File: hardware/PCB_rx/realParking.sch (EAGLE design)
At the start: 14 parts, among them IC1 MEGA8-P, IC2 LD117AV

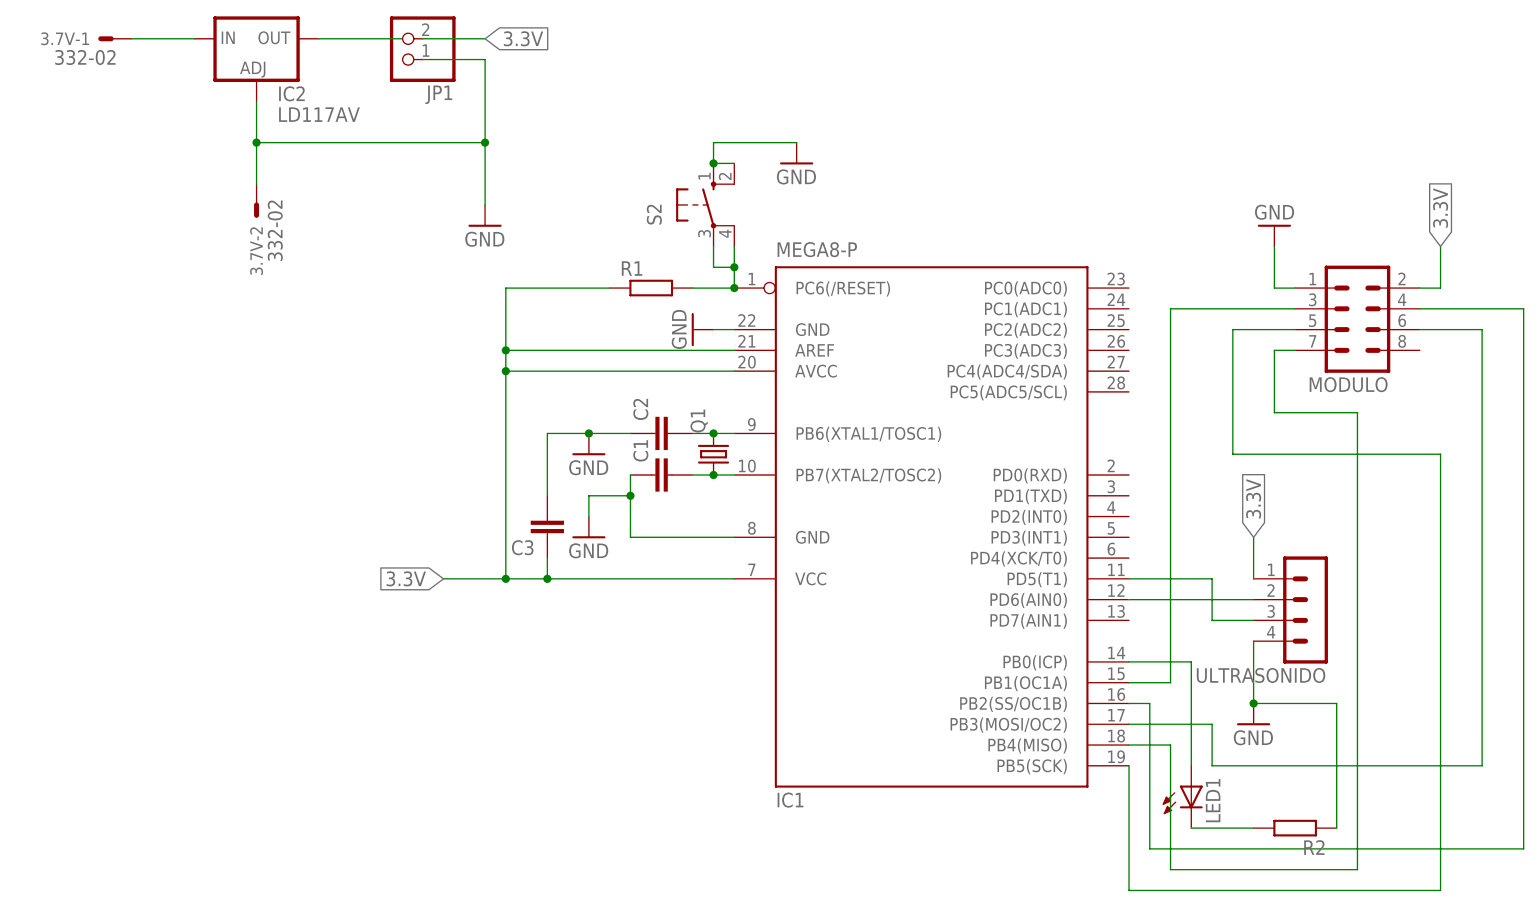
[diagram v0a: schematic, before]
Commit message: Se arregla diseño PCB del modulo transmisor
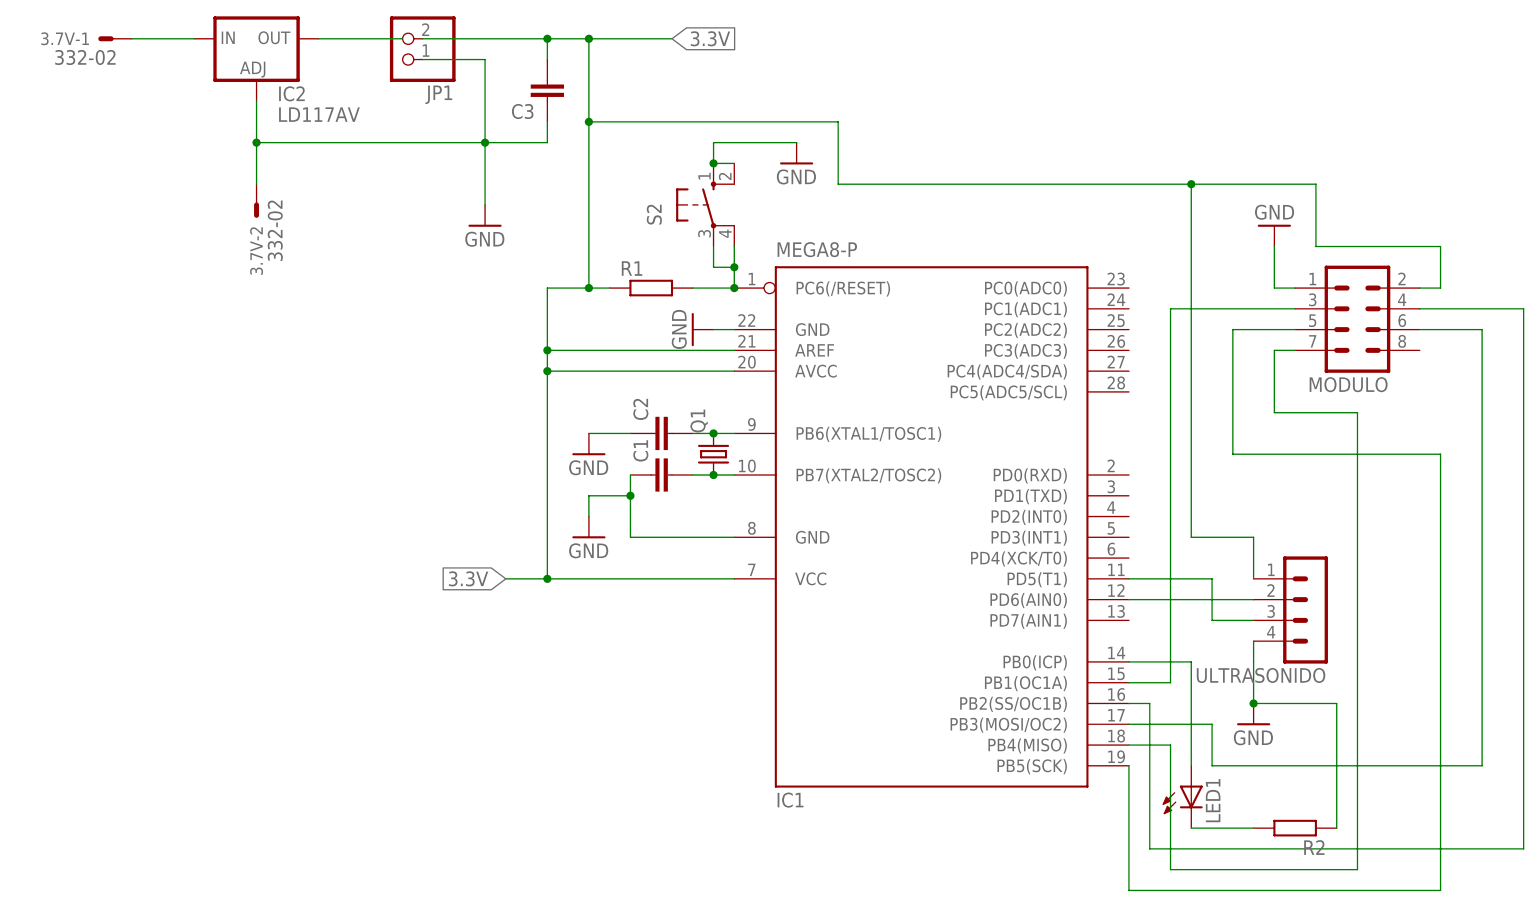
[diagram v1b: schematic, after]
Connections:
- removed net N$5: ULTRASONIDO.1
- removed net N$7: MODULO.2
- net 3.3V: now also C3.2, MODULO.2, ULTRASONIDO.1; no longer C3.1
- net GND: now also C3.1; no longer C3.2
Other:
- moved on the sheet: C3
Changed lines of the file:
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@@
 <instance part="C1" gate="G$1" x="20.32" y="60.96" rot="R90"/>
 <instance part="C2" gate="G$1" x="20.32" y="66.04" rot="R90"/>
-<instance part="C3" gate="G$1" x="7.62" y="53.34" rot="R180"/>
+<instance part="C3" gate="G$1" x="7.62" y="106.68" rot="R180"/>
 <instance part="S2" gate="1" x="27.94" y="93.98"/>
 <instance part="GND6" gate="1" x="25.4" y="78.74" rot="R270"/>
@@
 <wire x1="17.78" y1="66.04" x2="12.7" y2="66.04" width="0.1524" layer="91"/>
 <pinref part="C2" gate="G$1" pin="1"/>
-<pinref part="C3" gate="G$1" pin="2"/>
-<wire x1="7.62" y1="58.42" x2="7.62" y2="66.04" width="0.1524" layer="91"/>
-<wire x1="7.62" y1="66.04" x2="12.7" y2="66.04" width="0.1524" layer="91"/>
-<junction x="12.7" y="66.04"/>
 </segment>
 <segment>
@@
 <junction x="-27.94" y="101.6"/>
 <junction x="0" y="101.6"/>
+<pinref part="C3" gate="G$1" pin="1"/>
+<wire x1="7.62" y1="104.14" x2="7.62" y2="101.6" width="0.1524" layer="91"/>
+<wire x1="7.62" y1="101.6" x2="0" y2="101.6" width="0.1524" layer="91"/>
 </segment>
 <segment>
@@
 <pinref part="ULTRASONIDO" gate="1" pin="4"/>
 <pinref part="GND3" gate="1" pin="GND"/>
-<wire x1="93.98" y1="40.64" x2="93.98" y2="33.02" width="0.1524" layer="91"/>
 <pinref part="R2" gate="G$1" pin="1"/>
+<wire x1="93.98" y1="38.1" x2="93.98" y2="33.02" width="0.1524" layer="91"/>
 <wire x1="104.14" y1="17.78" x2="104.14" y2="33.02" width="0.1524" layer="91"/>
 <wire x1="104.14" y1="33.02" x2="93.98" y2="33.02" width="0.1524" layer="91"/>
 <junction x="93.98" y="33.02"/>
+<wire x1="93.98" y1="40.64" x2="93.98" y2="38.1" width="0.1524" layer="91"/>
 </segment>
 <segment>
@@
 <pinref part="IC1" gate="G$1" pin="AVCC"/>
 <wire x1="7.62" y1="48.26" x2="2.54" y2="48.26" width="0.1524" layer="91"/>
-<wire x1="2.54" y1="48.26" x2="-5.08" y2="48.26" width="0.1524" layer="91"/>
-<wire x1="30.48" y1="73.66" x2="2.54" y2="73.66" width="0.1524" layer="91"/>
-<wire x1="2.54" y1="73.66" x2="2.54" y2="48.26" width="0.1524" layer="91"/>
-<junction x="2.54" y="48.26"/>
+<wire x1="30.48" y1="73.66" x2="7.62" y2="73.66" width="0.1524" layer="91"/>
+<wire x1="7.62" y1="73.66" x2="7.62" y2="48.26" width="0.1524" layer="91"/>
+<junction x="7.62" y="48.26"/>
 <pinref part="IC1" gate="G$1" pin="AREF"/>
-<wire x1="30.48" y1="76.2" x2="2.54" y2="76.2" width="0.1524" layer="91"/>
-<wire x1="2.54" y1="76.2" x2="2.54" y2="73.66" width="0.1524" layer="91"/>
-<junction x="2.54" y="73.66"/>
-<wire x1="7.62" y1="50.8" x2="7.62" y2="48.26" width="0.1524" layer="91"/>
-<junction x="7.62" y="48.26"/>
-<pinref part="C3" gate="G$1" pin="1"/>
-<label x="-5.08" y="48.26" size="1.778" layer="95" rot="R180" xref="yes"/>
+<wire x1="30.48" y1="76.2" x2="7.62" y2="76.2" width="0.1524" layer="91"/>
+<wire x1="7.62" y1="76.2" x2="7.62" y2="73.66" width="0.1524" layer="91"/>
+<junction x="7.62" y="73.66"/>
+<label x="2.54" y="48.26" size="1.778" layer="95" rot="R180" xref="yes"/>
 <pinref part="R1" gate="G$1" pin="1"/>
-<wire x1="15.24" y1="83.82" x2="2.54" y2="83.82" width="0.1524" layer="91"/>
-<wire x1="2.54" y1="83.82" x2="2.54" y2="76.2" width="0.1524" layer="91"/>
-<junction x="2.54" y="76.2"/>
-<label x="93.98" y="53.34" size="1.778" layer="95" rot="R90" xref="yes"/>
-<label x="116.84" y="88.9" size="1.778" layer="95" rot="R90" xref="yes"/>
-</segment>
-<segment>
+<wire x1="15.24" y1="83.82" x2="12.7" y2="83.82" width="0.1524" layer="91"/>
+<wire x1="12.7" y1="83.82" x2="7.62" y2="83.82" width="0.1524" layer="91"/>
+<wire x1="7.62" y1="83.82" x2="7.62" y2="76.2" width="0.1524" layer="91"/>
+<junction x="7.62" y="76.2"/>
+<pinref part="MODULO" gate="G$1" pin="2"/>
+<wire x1="114.3" y1="83.82" x2="116.84" y2="83.82" width="0.1524" layer="91"/>
+<wire x1="116.84" y1="83.82" x2="116.84" y2="88.9" width="0.1524" layer="91"/>
+<wire x1="116.84" y1="88.9" x2="101.6" y2="88.9" width="0.1524" layer="91"/>
+<wire x1="101.6" y1="88.9" x2="101.6" y2="96.52" width="0.1524" layer="91"/>
+<wire x1="101.6" y1="96.52" x2="86.36" y2="96.52" width="0.1524" layer="91"/>
+<wire x1="86.36" y1="96.52" x2="43.18" y2="96.52" width="0.1524" layer="91"/>
+<wire x1="43.18" y1="96.52" x2="43.18" y2="104.14" width="0.1524" layer="91"/>
+<wire x1="43.18" y1="104.14" x2="12.7" y2="104.14" width="0.1524" layer="91"/>
+<wire x1="12.7" y1="104.14" x2="12.7" y2="83.82" width="0.1524" layer="91"/>
+<junction x="12.7" y="83.82"/>
+<pinref part="ULTRASONIDO" gate="1" pin="1"/>
+<wire x1="93.98" y1="48.26" x2="93.98" y2="53.34" width="0.1524" layer="91"/>
+<wire x1="93.98" y1="53.34" x2="86.36" y2="53.34" width="0.1524" layer="91"/>
+<wire x1="86.36" y1="53.34" x2="86.36" y2="96.52" width="0.1524" layer="91"/>
+<junction x="86.36" y="96.52"/>
 <pinref part="JP1" gate="G$1" pin="2"/>
-<wire x1="-7.62" y1="114.3" x2="0" y2="114.3" width="0.1524" layer="91"/>
-<label x="0" y="114.3" size="1.778" layer="95" xref="yes"/>
+<wire x1="-7.62" y1="114.3" x2="7.62" y2="114.3" width="0.1524" layer="91"/>
+<label x="22.86" y="114.3" size="1.778" layer="95" xref="yes"/>
+<pinref part="C3" gate="G$1" pin="2"/>
+<wire x1="7.62" y1="114.3" x2="12.7" y2="114.3" width="0.1524" layer="91"/>
+<wire x1="12.7" y1="114.3" x2="22.86" y2="114.3" width="0.1524" layer="91"/>
+<wire x1="7.62" y1="111.76" x2="7.62" y2="114.3" width="0.1524" layer="91"/>
+<junction x="7.62" y="114.3"/>
+<wire x1="12.7" y1="104.14" x2="12.7" y2="114.3" width="0.1524" layer="91"/>
+<junction x="12.7" y="104.14"/>
+<junction x="12.7" y="114.3"/>
 </segment>
 </net>
@@
 </segment>
 </net>
-<net name="N$5" class="0">
-<segment>
-<pinref part="ULTRASONIDO" gate="1" pin="1"/>
-<wire x1="93.98" y1="48.26" x2="93.98" y2="53.34" width="0.1524" layer="91"/>
-</segment>
-</net>
 <net name="N$6" class="0">
 <segment>
@@
 </segment>
 </net>
-<net name="N$7" class="0">
-<segment>
-<pinref part="MODULO" gate="G$1" pin="2"/>
-<wire x1="114.3" y1="83.82" x2="116.84" y2="83.82" width="0.1524" layer="91"/>
-<wire x1="116.84" y1="83.82" x2="116.84" y2="88.9" width="0.1524" layer="91"/>
-</segment>
-</net>
